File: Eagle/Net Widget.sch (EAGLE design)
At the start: 17 parts, among them IC1 ATmega1284P

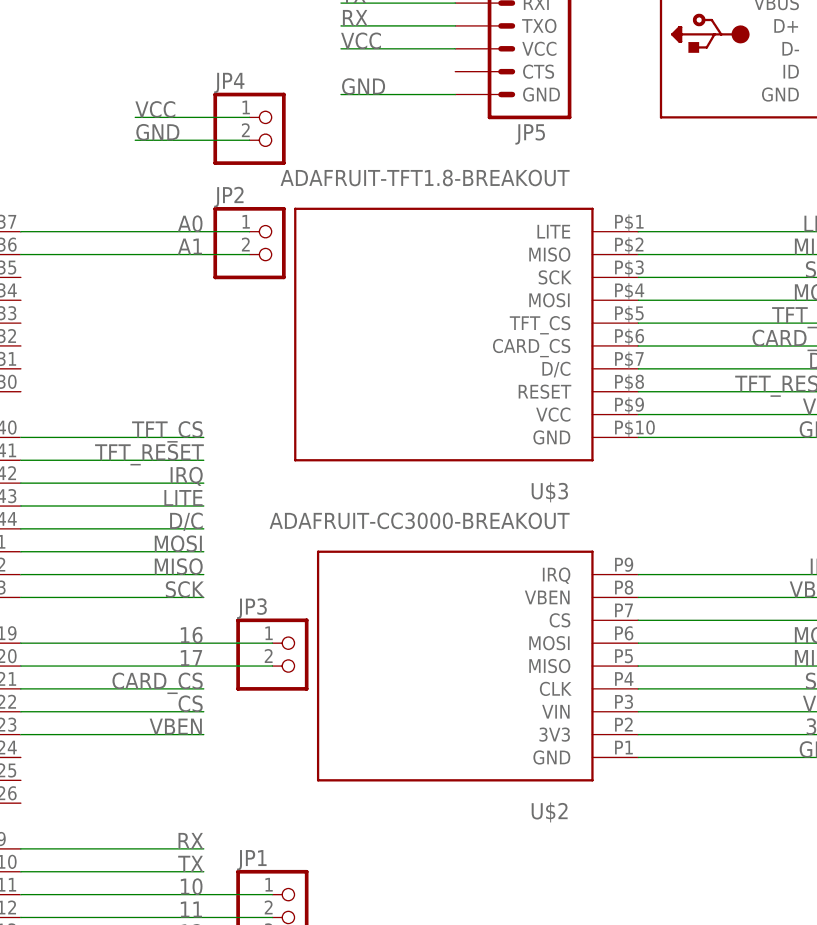
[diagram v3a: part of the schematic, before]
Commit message: SMD pads for breakout boards and layout.
Moved a bunch of things around after switching to right-angle
surface-mount headers for the CC3000 and TFT breakout boards.
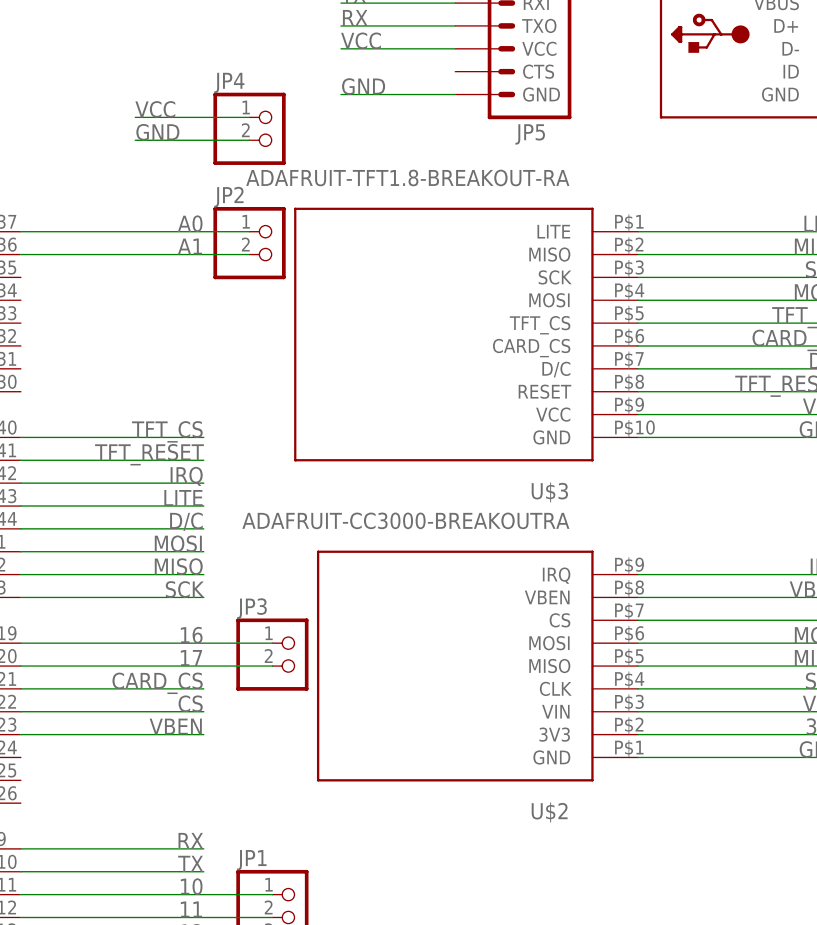
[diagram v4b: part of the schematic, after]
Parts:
- JP5: device Net Widget:ARDUINO_SERIAL_PROGRAMPTH -> SparkFun-Connectors:ARDUINO_SERIAL_PROGRAMSMD
- U$2: value ADAFRUIT-CC3000-BREAKOUT -> ADAFRUIT-CC3000-BREAKOUTRA; device Net Widget:ADAFRUIT-CC3000-BREAKOUT -> Net Widget:ADAFRUIT-CC3000-BREAKOUTRA
- U$3: value ADAFRUIT-TFT1.8-BREAKOUT -> ADAFRUIT-TFT1.8-BREAKOUT-RA; device Net Widget:ADAFRUIT-TFT1.8-BREAKOUT -> Net Widget:ADAFRUIT-TFT1.8-BREAKOUT-RA
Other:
- moved on the sheet: U$2
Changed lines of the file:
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@@
 </classes>
 <parts>
-<part name="U$2" library="Net Widget" deviceset="ADAFRUIT-CC3000-BREAKOUT" device=""/>
-<part name="U$3" library="Net Widget" deviceset="ADAFRUIT-TFT1.8-BREAKOUT" device=""/>
+<part name="U$2" library="Net Widget" deviceset="ADAFRUIT-CC3000-BREAKOUT" device="RA" value="ADAFRUIT-CC3000-BREAKOUTRA"/>
+<part name="U$3" library="Net Widget" deviceset="ADAFRUIT-TFT1.8-BREAKOUT" device="-RA" value="ADAFRUIT-TFT1.8-BREAKOUT-RA"/>
 <part name="ISP" library="adafruit" deviceset="AVRISP" device="-6"/>
 <part name="C2" library="rcl" deviceset="C-EU" device="C1206" value="18pF"/>
@@
 <part name="R4" library="rcl" deviceset="R-US_" device="R1206" value="10K"/>
 <part name="IC1" library="avr-5" deviceset="MEGA164P/324P/644P-AU" device="" value="ATmega1284P"/>
-<part name="JP5" library="Net Widget" deviceset="ARDUINO_SERIAL_PROGRAM" device="PTH" value="FTDI"/>
+<part name="JP5" library="SparkFun-Connectors" deviceset="ARDUINO_SERIAL_PROGRAM" device="SMD" value="FTDI"/>
 <part name="C1" library="rcl" deviceset="C-EU" device="C1206" value="0.1uF"/>
 <part name="JP1" library="pinhead" deviceset="PINHD-1X4" device=""/>

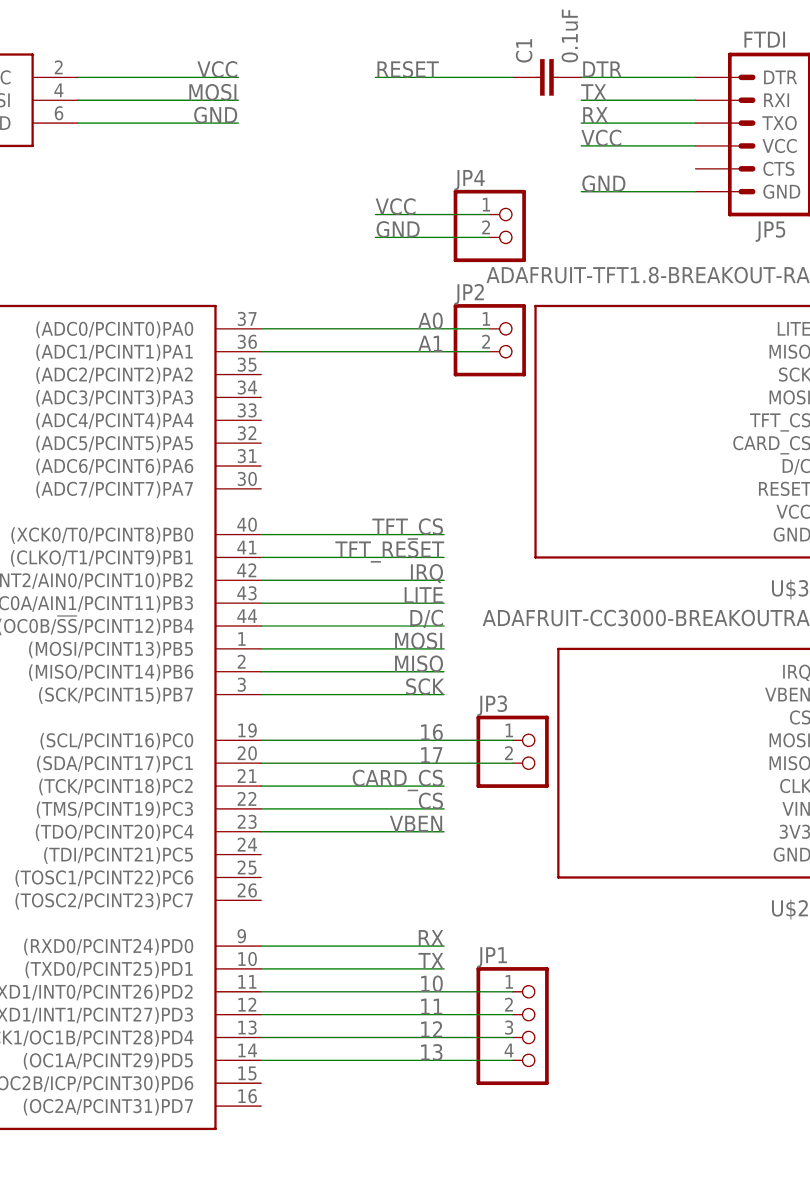
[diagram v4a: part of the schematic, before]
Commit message: Remove broken-out pins.
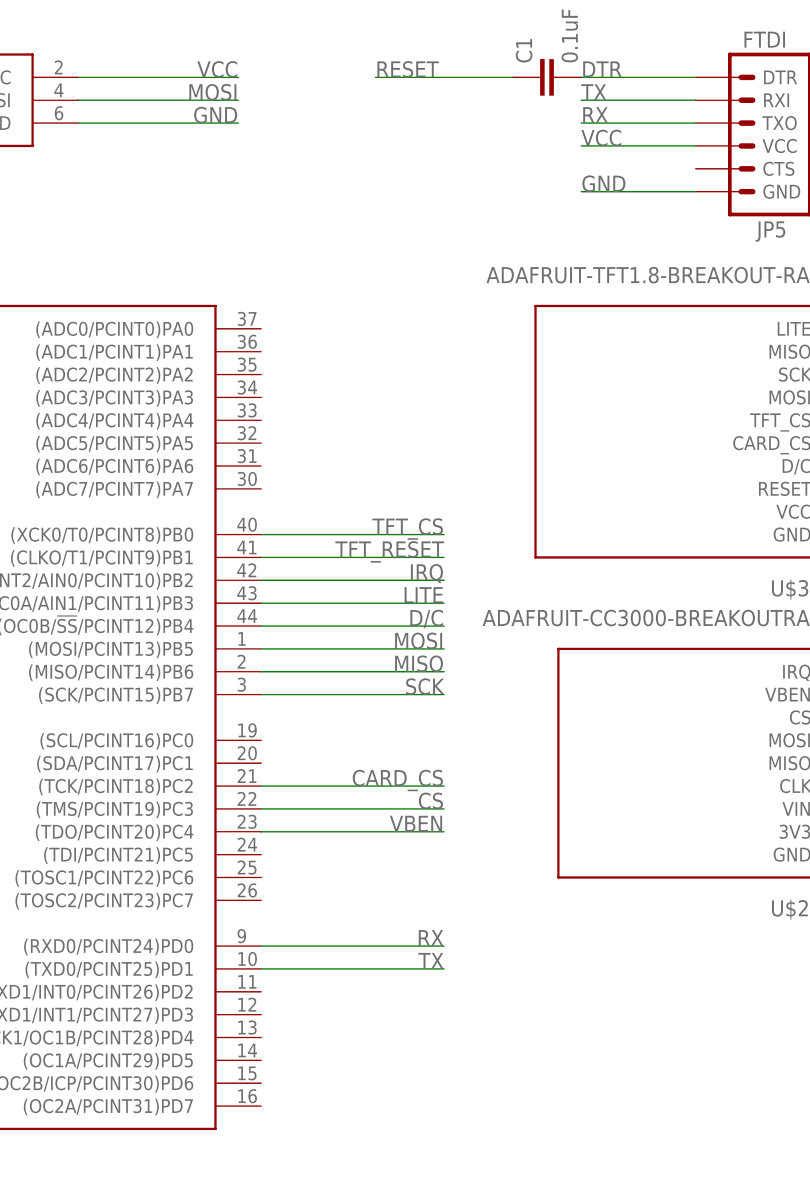
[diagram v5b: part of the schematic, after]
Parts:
- removed JP1: (no value), pinhead:PINHD-1X4
- removed JP2, JP3, JP4: (no value), pinhead:PINHD-1X2
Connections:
- removed net 10: IC1.(RXD1/INT0/PCINT26)PD2, JP1.1
- removed net 11: IC1.(TXD1/INT1/PCINT27)PD3, JP1.2
- removed net 12: IC1.(XCK1/OC1B/PCINT28)PD4, JP1.3
- removed net 13: IC1.(OC1A/PCINT29)PD5, JP1.4
- removed net 16: IC1.(SCL/PCINT16)PC0, JP3.1
- removed net 17: IC1.(SDA/PCINT17)PC1, JP3.2
- removed net A0: IC1.(ADC0/PCINT0)PA0, JP2.1
- removed net A1: IC1.(ADC1/PCINT1)PA1, JP2.2
- net GND: no longer JP4.2
- net VCC: no longer JP4.1
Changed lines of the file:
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@@
 <part name="C5" library="rcl" deviceset="C-EU" device="C1206" value="0.1uF"/>
 <part name="16MHZ" library="Net Widget" deviceset="CRYSTAL" device=""/>
-<part name="JP4" library="pinhead" deviceset="PINHD-1X2" device=""/>
 <part name="R4" library="rcl" deviceset="R-US_" device="R1206" value="10K"/>
 <part name="IC1" library="avr-5" deviceset="MEGA164P/324P/644P-AU" device="" value="ATmega1284P"/>
 <part name="JP5" library="SparkFun-Connectors" deviceset="ARDUINO_SERIAL_PROGRAM" device="SMD" value="FTDI"/>
 <part name="C1" library="rcl" deviceset="C-EU" device="C1206" value="0.1uF"/>
-<part name="JP1" library="pinhead" deviceset="PINHD-1X4" device=""/>
-<part name="JP2" library="pinhead" deviceset="PINHD-1X2" device=""/>
-<part name="JP3" library="pinhead" deviceset="PINHD-1X2" device=""/>
 <part name="CN1" library="Net Widget" deviceset="USB" device="PWR"/>
 </parts>
@@
 <instance part="C5" gate="G$1" x="193.04" y="104.14"/>
 <instance part="16MHZ" gate="G$1" x="27.94" y="71.12" rot="R90"/>
-<instance part="JP4" gate="G$1" x="111.76" y="91.44"/>
 <instance part="R4" gate="G$1" x="10.16" y="81.28" rot="R180"/>
 <instance part="IC1" gate="G$1" x="58.42" y="38.1"/>
 <instance part="JP5" gate="G$1" x="137.16" y="104.14" rot="R180"/>
 <instance part="C1" gate="G$1" x="114.3" y="109.22" rot="R90"/>
-<instance part="JP1" gate="A" x="114.3" y="2.54"/>
-<instance part="JP2" gate="G$1" x="111.76" y="78.74"/>
-<instance part="JP3" gate="G$1" x="114.3" y="33.02"/>
 <instance part="CN1" gate="G$1" x="165.1" y="101.6"/>
 </instances>
@@
 <junction x="185.42" y="96.52"/>
 <pinref part="CN1" gate="G$1" pin="GND"/>
-</segment>
-<segment>
-<pinref part="JP4" gate="G$1" pin="2"/>
-<wire x1="109.22" y1="91.44" x2="96.52" y2="91.44" width="0.1524" layer="91"/>
-<label x="96.52" y="91.44" size="1.778" layer="95"/>
 </segment>
 <segment>
@@
 <label x="175.26" y="27.94" size="1.778" layer="95" rot="MR0"/>
 <pinref part="U$2" gate="G$1" pin="VIN"/>
-</segment>
-<segment>
-<pinref part="JP4" gate="G$1" pin="1"/>
-<wire x1="109.22" y1="93.98" x2="96.52" y2="93.98" width="0.1524" layer="91"/>
-<label x="96.52" y="93.98" size="1.778" layer="95"/>
 </segment>
 <segment>
@@
 </segment>
 </net>
-<net name="A1" class="0">
-<segment>
-<pinref part="IC1" gate="G$1" pin="(ADC1/PCINT1)PA1"/>
-<wire x1="83.82" y1="78.74" x2="109.22" y2="78.74" width="0.1524" layer="91"/>
-<label x="104.14" y="78.74" size="1.778" layer="95" rot="MR0"/>
-<pinref part="JP2" gate="G$1" pin="2"/>
-</segment>
-</net>
-<net name="A0" class="0">
-<segment>
-<pinref part="IC1" gate="G$1" pin="(ADC0/PCINT0)PA0"/>
-<wire x1="83.82" y1="81.28" x2="109.22" y2="81.28" width="0.1524" layer="91"/>
-<label x="104.14" y="81.28" size="1.778" layer="95" rot="MR0"/>
-<pinref part="JP2" gate="G$1" pin="1"/>
-</segment>
-</net>
 <net name="DTR" class="0">
 <segment>
@@
 </segment>
 </net>
-<net name="10" class="0">
-<segment>
-<pinref part="IC1" gate="G$1" pin="(RXD1/INT0/PCINT26)PD2"/>
-<pinref part="JP1" gate="A" pin="1"/>
-<wire x1="111.76" y1="7.62" x2="83.82" y2="7.62" width="0.1524" layer="91"/>
-<label x="104.14" y="7.62" size="1.778" layer="95" rot="MR0"/>
-</segment>
-</net>
-<net name="11" class="0">
-<segment>
-<pinref part="IC1" gate="G$1" pin="(TXD1/INT1/PCINT27)PD3"/>
-<pinref part="JP1" gate="A" pin="2"/>
-<wire x1="111.76" y1="5.08" x2="83.82" y2="5.08" width="0.1524" layer="91"/>
-<label x="104.14" y="5.08" size="1.778" layer="95" rot="MR0"/>
-</segment>
-</net>
-<net name="12" class="0">
-<segment>
-<pinref part="IC1" gate="G$1" pin="(XCK1/OC1B/PCINT28)PD4"/>
-<pinref part="JP1" gate="A" pin="3"/>
-<wire x1="111.76" y1="2.54" x2="83.82" y2="2.54" width="0.1524" layer="91"/>
-<label x="104.14" y="2.54" size="1.778" layer="95" rot="MR0"/>
-</segment>
-</net>
-<net name="13" class="0">
-<segment>
-<pinref part="IC1" gate="G$1" pin="(OC1A/PCINT29)PD5"/>
-<pinref part="JP1" gate="A" pin="4"/>
-<wire x1="111.76" y1="0" x2="83.82" y2="0" width="0.1524" layer="91"/>
-<label x="104.14" y="0" size="1.778" layer="95" rot="MR0"/>
-</segment>
-</net>
-<net name="16" class="0">
-<segment>
-<pinref part="IC1" gate="G$1" pin="(SCL/PCINT16)PC0"/>
-<pinref part="JP3" gate="G$1" pin="1"/>
-<wire x1="111.76" y1="35.56" x2="83.82" y2="35.56" width="0.1524" layer="91"/>
-<label x="104.14" y="35.56" size="1.778" layer="95" rot="MR0"/>
-</segment>
-</net>
-<net name="17" class="0">
-<segment>
-<pinref part="IC1" gate="G$1" pin="(SDA/PCINT17)PC1"/>
-<pinref part="JP3" gate="G$1" pin="2"/>
-<wire x1="111.76" y1="33.02" x2="83.82" y2="33.02" width="0.1524" layer="91"/>
-<label x="104.14" y="33.02" size="1.778" layer="95" rot="MR0"/>
-</segment>
-</net>

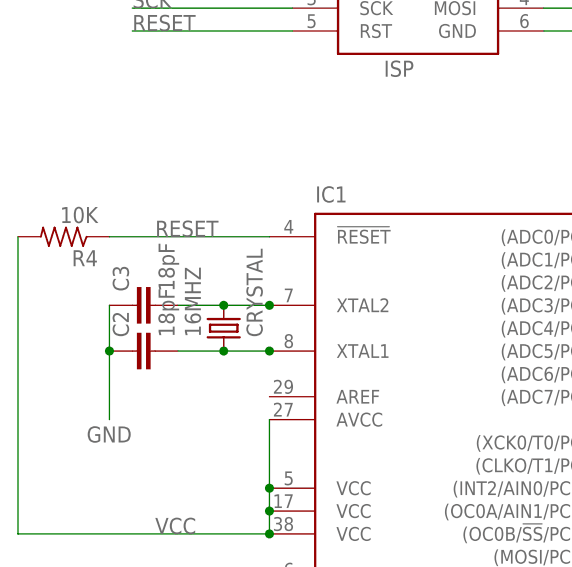
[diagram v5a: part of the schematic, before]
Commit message: Move CC3000, re-route, silk screen cleanup.
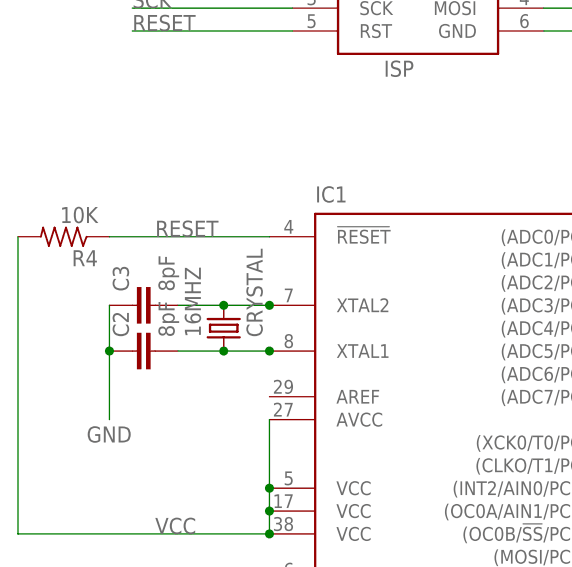
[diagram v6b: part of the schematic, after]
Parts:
- C2, C3: value 18pF -> 8pF
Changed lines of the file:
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@@
 <part name="U$3" library="Net Widget" deviceset="ADAFRUIT-TFT1.8-BREAKOUT" device="-RA" value="ADAFRUIT-TFT1.8-BREAKOUT-RA"/>
 <part name="ISP" library="adafruit" deviceset="AVRISP" device="-6"/>
-<part name="C2" library="rcl" deviceset="C-EU" device="C1206" value="18pF"/>
-<part name="C3" library="rcl" deviceset="C-EU" device="C1206" value="18pF"/>
+<part name="C2" library="rcl" deviceset="C-EU" device="C1206" value="8pF"/>
+<part name="C3" library="rcl" deviceset="C-EU" device="C1206" value="8pF"/>
 <part name="C4" library="rcl" deviceset="C-EU" device="C1206" value="10uF"/>
 <part name="C5" library="rcl" deviceset="C-EU" device="C1206" value="0.1uF"/>

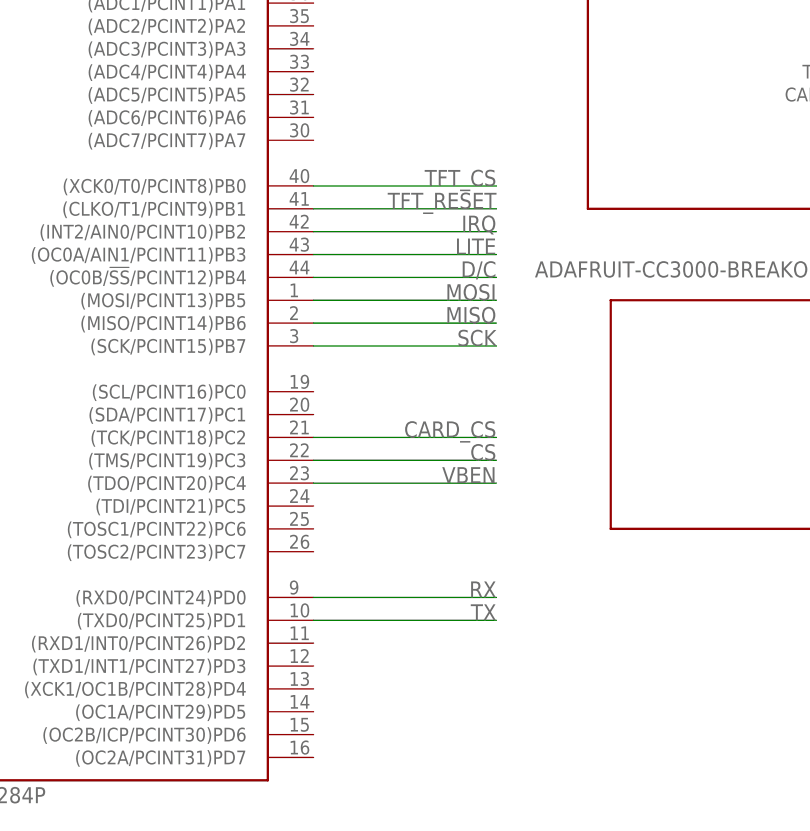
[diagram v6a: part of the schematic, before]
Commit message: Match pin numbers to WildFire; route.
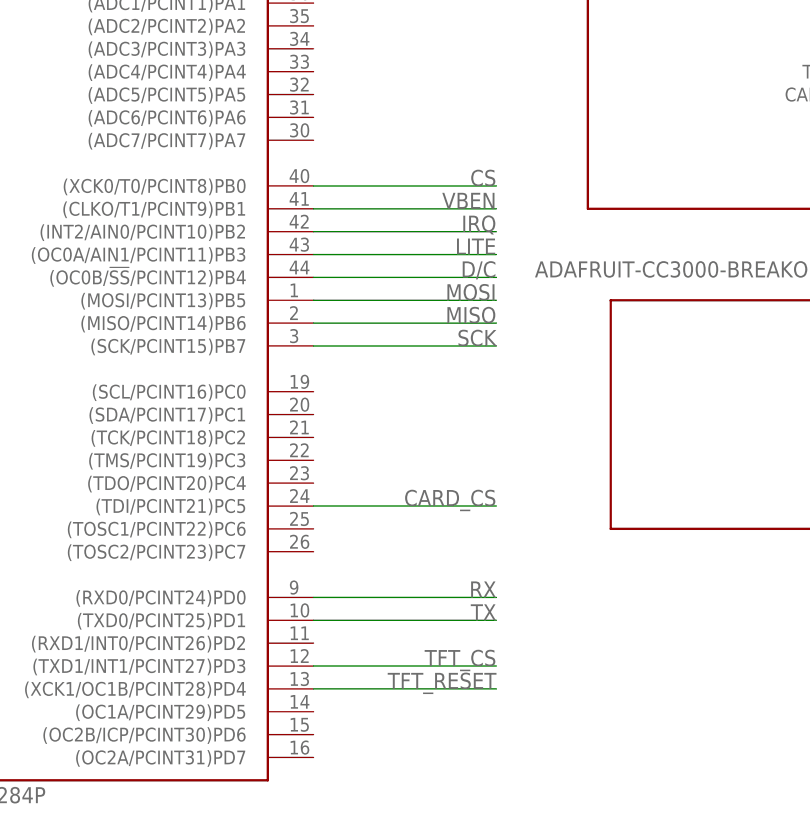
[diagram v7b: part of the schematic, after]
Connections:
- net CARD_CS: now also IC1.(TDI/PCINT21)PC5; no longer IC1.(TCK/PCINT18)PC2
- net CS: now also IC1.(XCK0/T0/PCINT8)PB0; no longer IC1.(TMS/PCINT19)PC3
- net TFT_CS: now also IC1.(TXD1/INT1/PCINT27)PD3; no longer IC1.(XCK0/T0/PCINT8)PB0
- net TFT_RESET: now also IC1.(XCK1/OC1B/PCINT28)PD4; no longer IC1.(CLKO/T1/PCINT9)PB1
- net VBEN: now also IC1.(CLKO/T1/PCINT9)PB1; no longer IC1.(TDO/PCINT20)PC4
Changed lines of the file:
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@@
 </segment>
 <segment>
-<pinref part="IC1" gate="G$1" pin="(TCK/PCINT18)PC2"/>
-<wire x1="83.82" y1="30.48" x2="104.14" y2="30.48" width="0.1524" layer="91"/>
-<label x="104.14" y="30.48" size="1.778" layer="95" rot="MR0"/>
+<pinref part="IC1" gate="G$1" pin="(TDI/PCINT21)PC5"/>
+<wire x1="83.82" y1="22.86" x2="104.14" y2="22.86" width="0.1524" layer="91"/>
+<label x="104.14" y="22.86" size="1.778" layer="95" rot="MR0"/>
 </segment>
 </net>
@@
 </segment>
 <segment>
-<pinref part="IC1" gate="G$1" pin="(XCK0/T0/PCINT8)PB0"/>
-<wire x1="83.82" y1="58.42" x2="104.14" y2="58.42" width="0.1524" layer="91"/>
-<label x="104.14" y="58.42" size="1.778" layer="95" rot="MR0"/>
+<pinref part="IC1" gate="G$1" pin="(TXD1/INT1/PCINT27)PD3"/>
+<wire x1="83.82" y1="5.08" x2="104.14" y2="5.08" width="0.1524" layer="91"/>
+<label x="104.14" y="5.08" size="1.778" layer="95" rot="MR0"/>
 </segment>
 </net>
@@
 </segment>
 <segment>
-<pinref part="IC1" gate="G$1" pin="(TMS/PCINT19)PC3"/>
-<wire x1="83.82" y1="27.94" x2="104.14" y2="27.94" width="0.1524" layer="91"/>
-<label x="104.14" y="27.94" size="1.778" layer="95" rot="MR0"/>
+<pinref part="IC1" gate="G$1" pin="(XCK0/T0/PCINT8)PB0"/>
+<wire x1="83.82" y1="58.42" x2="104.14" y2="58.42" width="0.1524" layer="91"/>
+<label x="104.14" y="58.42" size="1.778" layer="95" rot="MR0"/>
 </segment>
 </net>
@@
 </segment>
 <segment>
-<pinref part="IC1" gate="G$1" pin="(TDO/PCINT20)PC4"/>
-<wire x1="83.82" y1="25.4" x2="104.14" y2="25.4" width="0.1524" layer="91"/>
-<label x="104.14" y="25.4" size="1.778" layer="95" rot="MR0"/>
+<pinref part="IC1" gate="G$1" pin="(CLKO/T1/PCINT9)PB1"/>
+<wire x1="83.82" y1="55.88" x2="104.14" y2="55.88" width="0.1524" layer="91"/>
+<label x="104.14" y="55.88" size="1.778" layer="95" rot="MR0"/>
 </segment>
 </net>
@@
 </segment>
 <segment>
-<pinref part="IC1" gate="G$1" pin="(CLKO/T1/PCINT9)PB1"/>
-<wire x1="83.82" y1="55.88" x2="104.14" y2="55.88" width="0.1524" layer="91"/>
-<label x="104.14" y="55.88" size="1.778" layer="95" rot="MR0"/>
+<pinref part="IC1" gate="G$1" pin="(XCK1/OC1B/PCINT28)PD4"/>
+<wire x1="83.82" y1="2.54" x2="104.14" y2="2.54" width="0.1524" layer="91"/>
+<label x="104.14" y="2.54" size="1.778" layer="95" rot="MR0"/>
 </segment>
 </net>
